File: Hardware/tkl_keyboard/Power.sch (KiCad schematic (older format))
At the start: 13 parts, among them J7 Barrel_Jack_MountingPin, J8 Conn_01x03_Male, U2 ADP2303ARDZ-5.0, U9 TCR2EF33

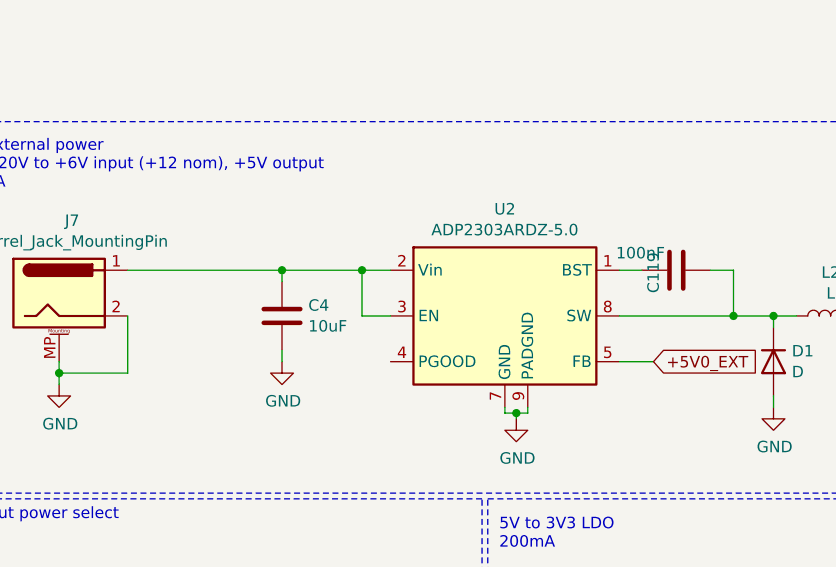
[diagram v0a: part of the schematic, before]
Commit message: Power supply routed
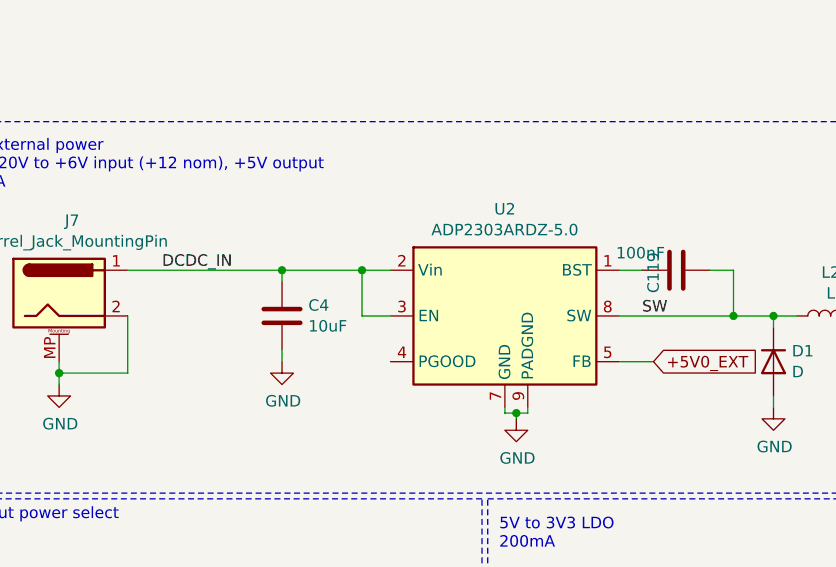
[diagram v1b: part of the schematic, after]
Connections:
- net DCDC_IN: now reaches C4.1, J7.1, U2.2 (Vin), U2.3 (EN)
- net SW: now reaches C119.2, D1.1 (K), L2.1, U2.8 (SW)
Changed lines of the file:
@@
 Wire Notes Line
 	5250 3900 3000 3900
+Text Label 3850 2900 0    50   ~ 0
+DCDC_IN
+Text Label 5950 3100 0    50   ~ 0
+SW
 $EndSCHEMATC

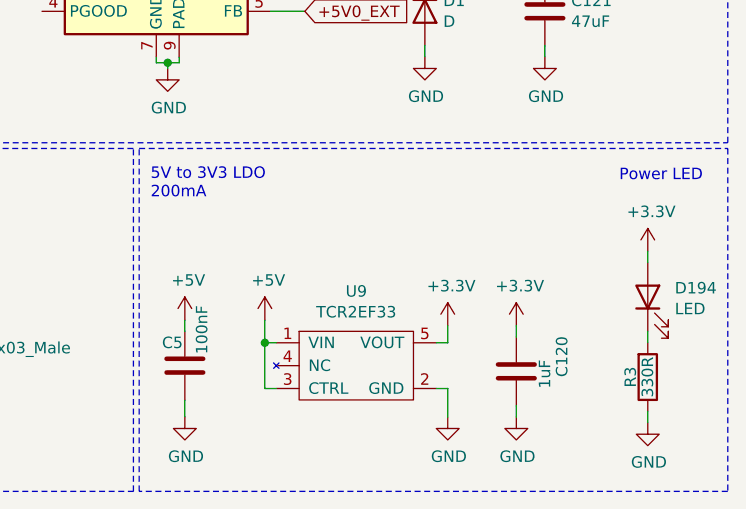
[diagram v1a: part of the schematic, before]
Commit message: First pass of routing done
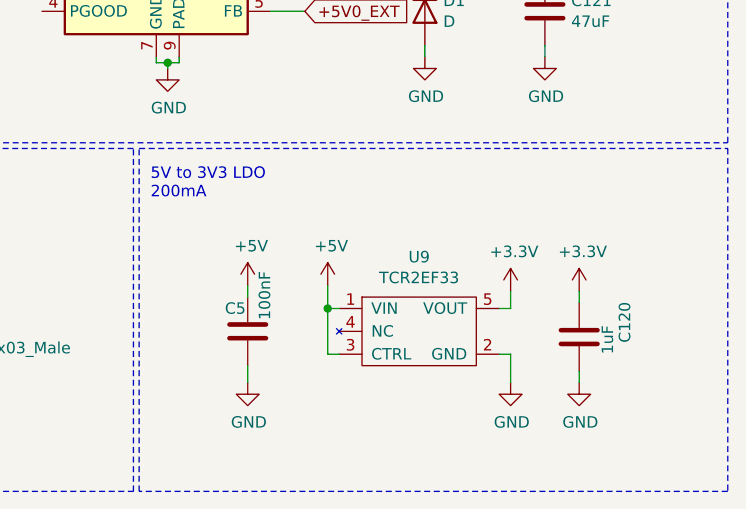
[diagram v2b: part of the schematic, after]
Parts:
- removed D194: LED, Diode_SMD:D_0603_1608Metric, symbol Device:LED
- removed R3: 330R, resistor_smd:R_0603_1608Metric, symbol Device:R
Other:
- note removed: "Power LED"
- moved on the sheet: C120, C5, U9

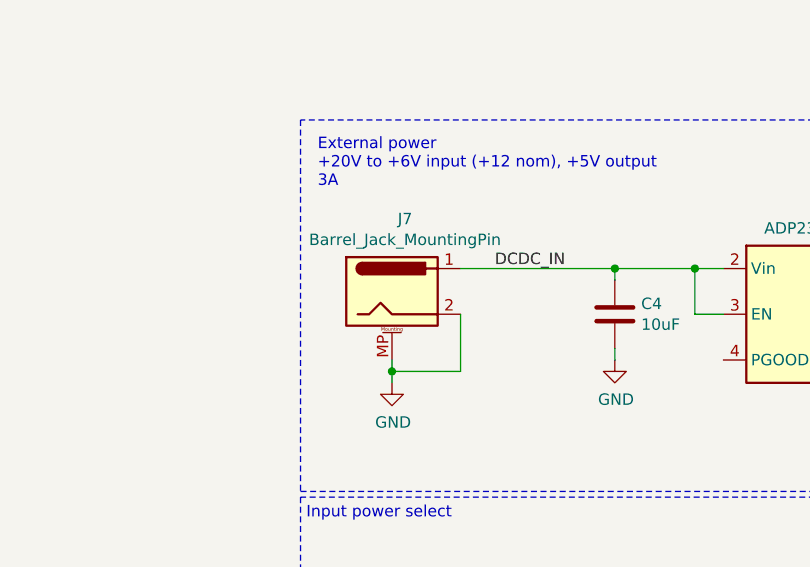
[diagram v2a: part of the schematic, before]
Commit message: Added some missing capacitors, Fixed DC jack footprint connections
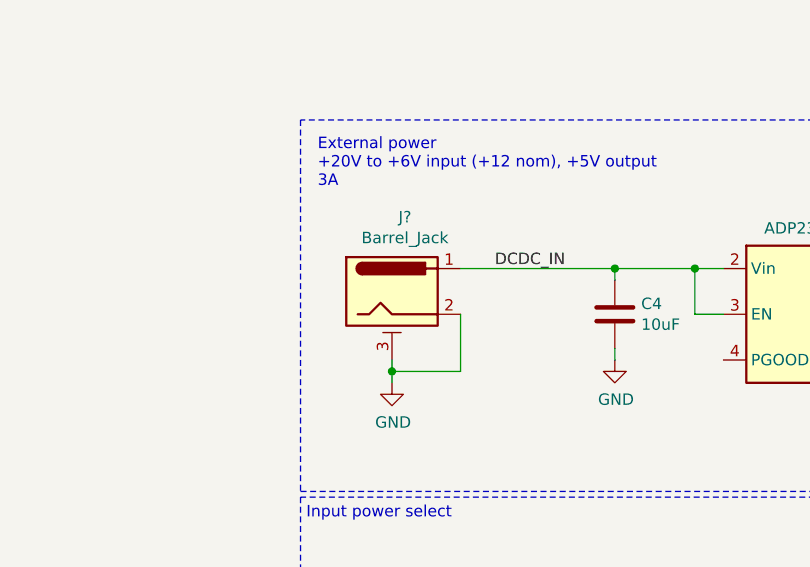
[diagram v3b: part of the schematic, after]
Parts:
- removed J7: Barrel_Jack_MountingPin, Connector_BarrelJack:BarrelJack_Wuerth_6941xx301002, symbol Connector:Barrel_Jack_MountingPin
- added J?: Barrel_Jack, symbol custom_parts_library:Barrel_Jack
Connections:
- net DCDC_IN: now also J?.1
- net GND: now also J?.2, J?.3
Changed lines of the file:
@@
-	1    0    0    -1
-$EndComp
-$Comp
-L Connector:Barrel_Jack_MountingPin J7
-U 1 1 6133B7B7
-P 3400 3000
-F 0 "J7" H 3457 3317 50  0000 C CNN
-F 1 "Barrel_Jack_MountingPin" H 3457 3226 50  0000 C CNN
-F 2 "Connector_BarrelJack:BarrelJack_Wuerth_6941xx301002" H 3450 2960 50  0001 C CNN
-F 3 "~" H 3450 2960 50  0001 C CNN
-	1    3400 3000
 	1    0    0    -1
 $EndComp
@@
 Text Label 5950 3100 0    50   ~ 0
 SW
+$Comp
+L custom_parts_library:Barrel_Jack J?
+U 1 1 61714EB0
+P 3400 3000
+F 0 "J?" H 3457 3325 50  0000 C CNN
+F 1 "Barrel_Jack" H 3457 3234 50  0000 C CNN
+F 2 "" H 2850 3350 50  0001 C CNN
+F 3 "" H 2850 3350 50  0001 C CNN
+	1    3400 3000
+	1    0    0    -1
+$EndComp
 $EndSCHEMATC

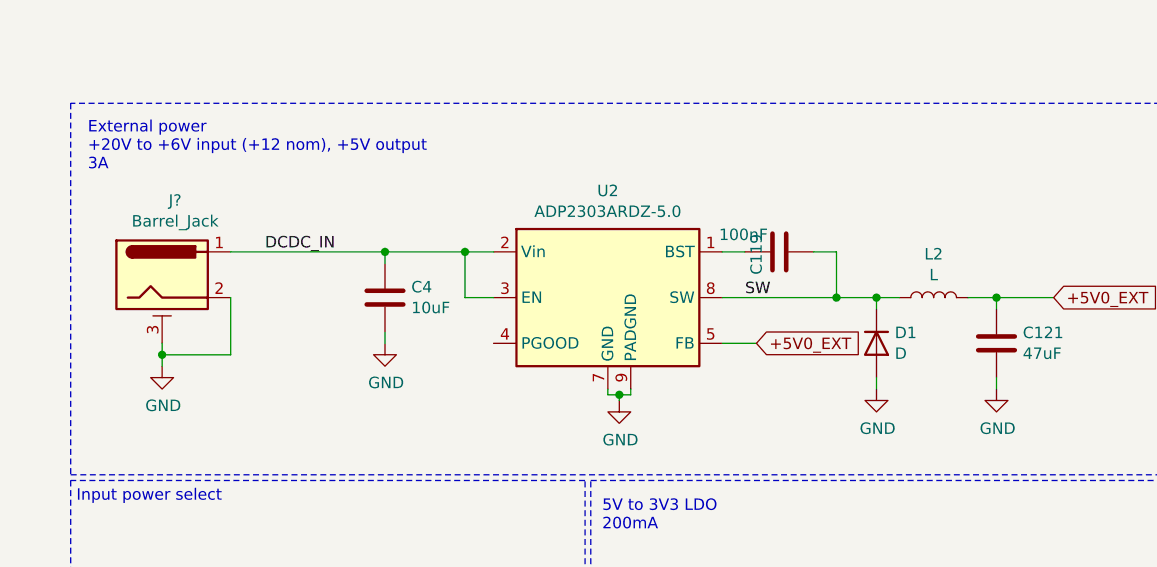
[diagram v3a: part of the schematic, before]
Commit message: Tidying schematic
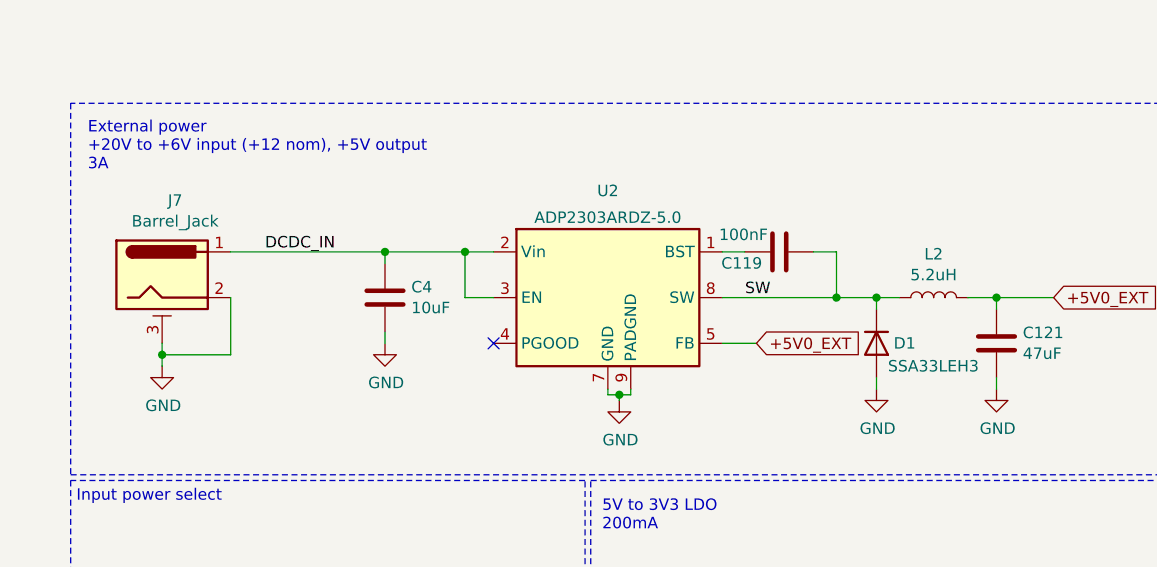
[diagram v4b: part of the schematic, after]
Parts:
- D1: value D -> SSA33LEH3
- J7: renamed from J?; footprint (none) -> Connector_BarrelJack:BarrelJack_Wuerth_6941xx301002
- L2: value L -> 5.2uH
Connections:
- no-connect marks 0 -> 1
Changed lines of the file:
@@
 encoding utf-8
 Sheet 12 12
-Title ""
+Title "TKL Keyboard"
 Date ""
-Rev ""
+Rev "0"
 Comp ""
 Comment1 ""
@@
 Text Notes 750  1000 0    315  ~ 0
 Power
-$Comp
-L Regulator_Switching:ADP2303ARDZ-5.0 U2
-U 1 1 613398E3
-P 5350 3100
-F 0 "U2" H 5350 3567 50  0000 C CNN
-F 1 "ADP2303ARDZ-5.0" H 5350 3476 50  0000 C CNN
-F 2 "Package_SO:SOIC-8-1EP_3.9x4.9mm_P1.27mm_EP2.29x3mm" H 5500 2750 50  0001 L CNN
-F 3 "https://www.analog.com/media/en/technical-documentation/data-sheets/ADP2302_2303.pdf" H 5150 3700 50  0001 C CNN
-	1    5350 3100
-	1    0    0    -1
-$EndComp
 Wire Wire Line
 	3700 2900 4375 2900
@@
 	4725 2900 4850 2900
 $Comp
-L Device:L L2
-U 1 1 6133D48E
-P 6775 3100
-F 0 "L2" V 6965 3100 50  0000 C CNN
-F 1 "L" V 6874 3100 50  0000 C CNN
-F 2 "Inductor_SMD:L_10.4x10.4_H4.8" H 6775 3100 50  0001 C CNN
-F 3 "~" H 6775 3100 50  0001 C CNN
-	1    6775 3100
-	0    -1   -1   0
-$EndComp
-$Comp
 L Device:C C121
 U 1 1 6133DD37
@@
 	1    0    0    -1
 $EndComp
-$Comp
-L Device:D D1
-U 1 1 6133E473
-P 6525 3300
-F 0 "D1" V 6479 3380 50  0000 L CNN
-F 1 "D" V 6570 3380 50  0000 L CNN
-F 2 "custom_footprint_library:DO-214AC" H 6525 3300 50  0001 C CNN
-F 3 "~" H 6525 3300 50  0001 C CNN
-	1    6525 3300
-	0    1    1    0
-$EndComp
 Wire Wire Line
 	6525 3150 6525 3100
@@
 Wire Wire Line
 	5850 3100 6350 3100
-$Comp
-L Device:C C?
-U 1 1 6134519E
-P 6100 2900
-AR Path="/6134519E" Ref="C?"  Part="1"
-AR Path="/60D44BDB/6134519E" Ref="C?"  Part="1"
-AR Path="/60D99CF5/6134519E" Ref="C?"  Part="1"
-AR Path="/60D44364/6134519E" Ref="C?"  Part="1"
-AR Path="/61150193/6134519E" Ref="C?"  Part="1"
-AR Path="/61D5AB4C/6134519E" Ref="C?"  Part="1"
-AR Path="/6247A5CE/6134519E" Ref="C?"  Part="1"
-AR Path="/6114D32E/6134519E" Ref="C?"  Part="1"
-AR Path="/612340DE/6134519E" Ref="C?"  Part="1"
-AR Path="/62F6B81F/6134519E" Ref="C?"  Part="1"
-AR Path="/613390DE/6134519E" Ref="C119"  Part="1"
-F 0 "C119" H 6000 3000 50  0000 L CNN
-F 1 "100nF" V 6175 2950 50  0000 L CNN
-F 2 "Capacitor_smd:C_0603_1608Metric" H 6138 2750 50  0001 C CNN
-F 3 "~" H 6100 2900 50  0001 C CNN
-	1    6100 2900
-	0    -1   -1   0
-$EndComp
 Wire Wire Line
 	5850 2900 5950 2900
@@
 Wire Wire Line
 	3825 4850 4125 4850
-$Comp
-L custom_parts_library:TCR2EF33 U?
-U 1 1 61533A30
-P 6600 4900
-AR Path="/6114D32E/61533A30" Ref="U?"  Part="1"
-AR Path="/6247A5CE/61533A30" Ref="U?"  Part="1"
-AR Path="/612340DE/61533A30" Ref="U?"  Part="1"
-AR Path="/62F6B81F/61533A30" Ref="U?"  Part="1"
-AR Path="/613390DE/61533A30" Ref="U9"  Part="1"
-F 0 "U9" H 6500 5425 50  0000 C CNN
-F 1 "TCR2EF33" H 6500 5334 50  0000 C CNN
-F 2 "custom_footprint_library:TCR2EF33_SOT25" H 5800 5600 50  0001 C CNN
-F 3 "" H 5800 5600 50  0001 C CNN
-	1    6600 4900
-	1    0    0    -1
-$EndComp
 $Comp
 L power:+5V #PWR?
@@
 SW
 $Comp
-L custom_parts_library:Barrel_Jack J?
+L custom_parts_library:Barrel_Jack J7
 U 1 1 61714EB0
 P 3400 3000
-F 0 "J?" H 3457 3325 50  0000 C CNN
+F 0 "J7" H 3457 3325 50  0000 C CNN
 F 1 "Barrel_Jack" H 3457 3234 50  0000 C CNN
-F 2 "" H 2850 3350 50  0001 C CNN
+F 2 "Connector_BarrelJack:BarrelJack_Wuerth_6941xx301002" H 2850 3350 50  0001 C CNN
 F 3 "" H 2850 3350 50  0001 C CNN
 	1    3400 3000
 	1    0    0    -1
 $EndComp
+NoConn ~ 4850 3300
+$Comp
+L custom_parts_library:TCR2EF33 U?
+U 1 1 61533A30
+P 6600 4900
+AR Path="/6114D32E/61533A30" Ref="U?"  Part="1"
+AR Path="/6247A5CE/61533A30" Ref="U?"  Part="1"
+AR Path="/612340DE/61533A30" Ref="U?"  Part="1"
+AR Path="/62F6B81F/61533A30" Ref="U?"  Part="1"
+AR Path="/613390DE/61533A30" Ref="U9"  Part="1"
+F 0 "U9" H 6500 5425 50  0000 C CNN
+F 1 "TCR2EF33" H 6500 5334 50  0000 C CNN
+F 2 "custom_footprint_library:TCR2EF33_SOT25" H 5800 5600 50  0001 C CNN
+F 3 "" H 5800 5600 50  0001 C CNN
+	1    6600 4900
+	1    0    0    -1
+$EndComp
+$Comp
+L Device:D D1
+U 1 1 6133E473
+P 6525 3300
+F 0 "D1" V 6525 3375 50  0000 L CNN
+F 1 "SSA33LEH3" V 6625 3350 50  0000 L CNN
+F 2 "custom_footprint_library:DO-214AC" H 6525 3300 50  0001 C CNN
+F 3 "~" H 6525 3300 50  0001 C CNN
+	1    6525 3300
+	0    1    1    0
+$EndComp
+$Comp
+L Device:C C?
+U 1 1 6134519E
+P 6100 2900
+AR Path="/6134519E" Ref="C?"  Part="1"
+AR Path="/60D44BDB/6134519E" Ref="C?"  Part="1"
+AR Path="/60D99CF5/6134519E" Ref="C?"  Part="1"
+AR Path="/60D44364/6134519E" Ref="C?"  Part="1"
+AR Path="/61150193/6134519E" Ref="C?"  Part="1"
+AR Path="/61D5AB4C/6134519E" Ref="C?"  Part="1"
+AR Path="/6247A5CE/6134519E" Ref="C?"  Part="1"
+AR Path="/6114D32E/6134519E" Ref="C?"  Part="1"
+AR Path="/612340DE/6134519E" Ref="C?"  Part="1"
+AR Path="/62F6B81F/6134519E" Ref="C?"  Part="1"
+AR Path="/613390DE/6134519E" Ref="C119"  Part="1"
+F 0 "C119" V 6050 2975 50  0000 L CNN
+F 1 "100nF" V 6175 2950 50  0000 L CNN
+F 2 "Capacitor_smd:C_0603_1608Metric" H 6138 2750 50  0001 C CNN
+F 3 "~" H 6100 2900 50  0001 C CNN
+	1    6100 2900
+	0    -1   -1   0
+$EndComp
+$Comp
+L Regulator_Switching:ADP2303ARDZ-5.0 U2
+U 1 1 613398E3
+P 5350 3100
+F 0 "U2" H 5350 3567 50  0000 C CNN
+F 1 "ADP2303ARDZ-5.0" H 5350 3450 50  0000 C CNN
+F 2 "Package_SO:SOIC-8-1EP_3.9x4.9mm_P1.27mm_EP2.29x3mm" H 5500 2750 50  0001 L CNN
+F 3 "https://www.analog.com/media/en/technical-documentation/data-sheets/ADP2302_2303.pdf" H 5150 3700 50  0001 C CNN
+	1    5350 3100
+	1    0    0    -1
+$EndComp
+$Comp
+L Device:L L2
+U 1 1 6133D48E
+P 6775 3100
+F 0 "L2" V 6965 3100 50  0000 C CNN
+F 1 "5.2uH" V 6874 3100 50  0000 C CNN
+F 2 "Inductor_SMD:L_10.4x10.4_H4.8" H 6775 3100 50  0001 C CNN
+F 3 "~" H 6775 3100 50  0001 C CNN
+	1    6775 3100
+	0    -1   -1   0
+$EndComp
 $EndSCHEMATC
